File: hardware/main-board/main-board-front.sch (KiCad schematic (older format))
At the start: 25 parts

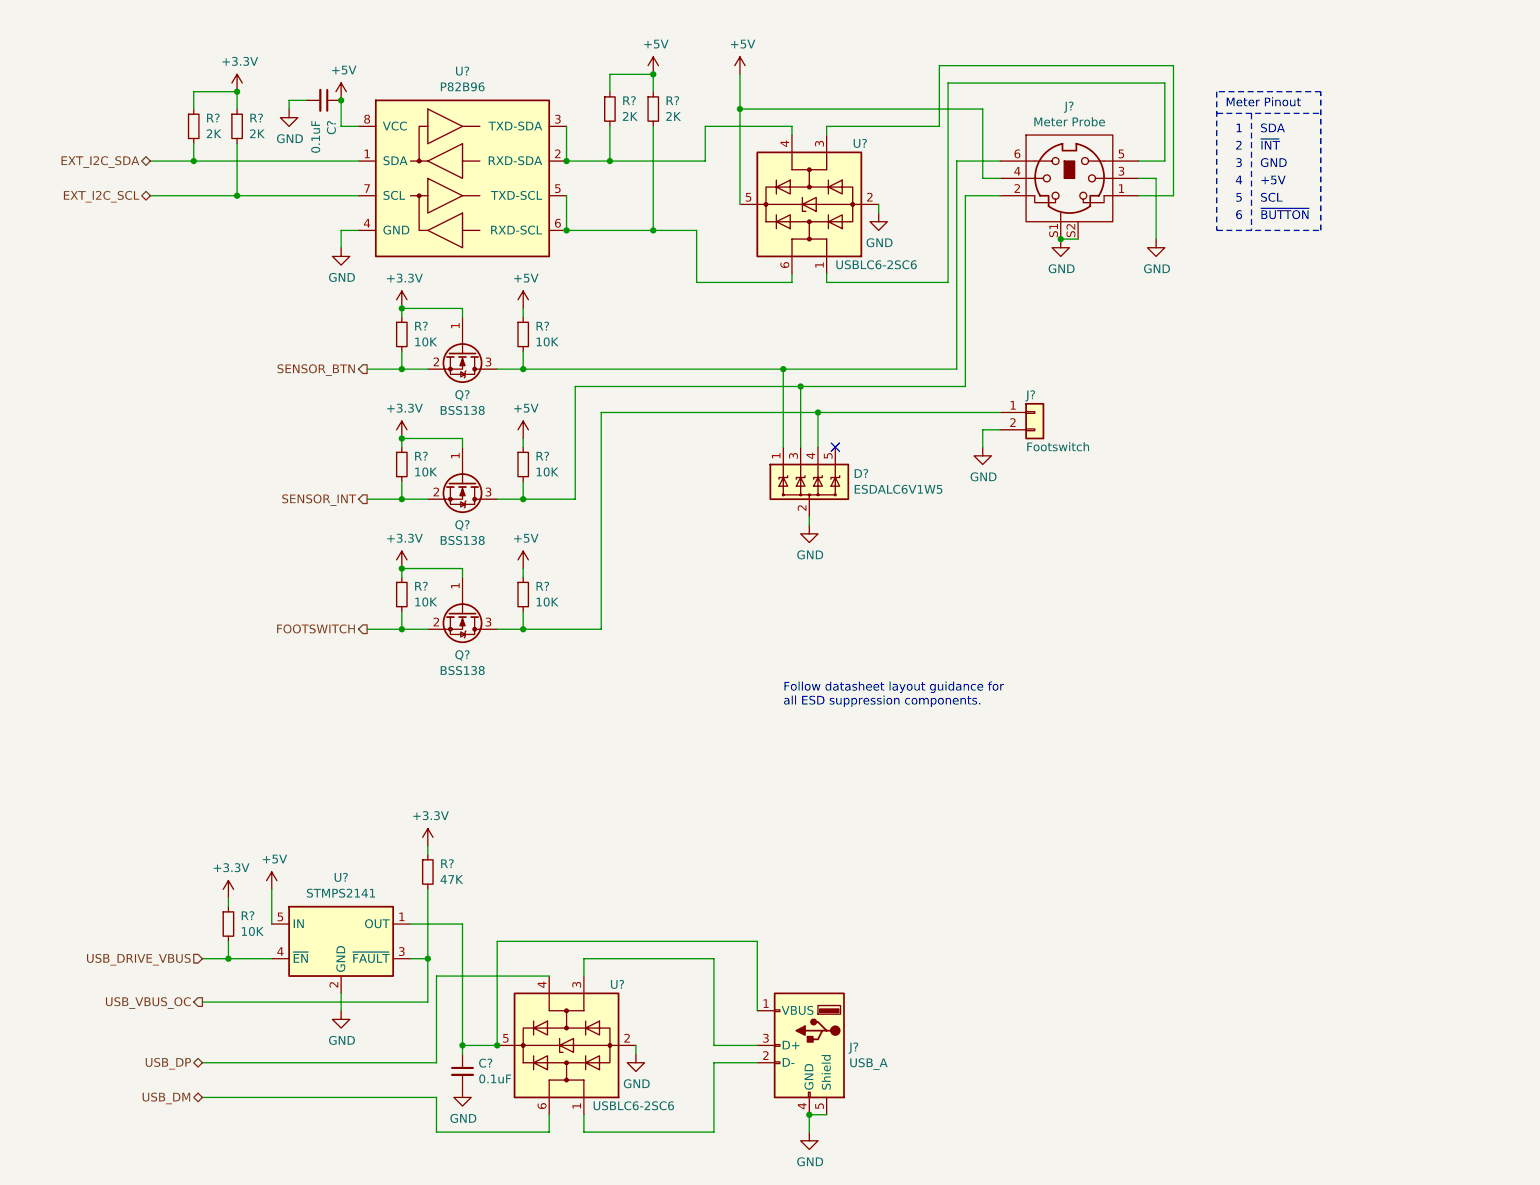
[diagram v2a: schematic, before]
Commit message: Annotated schematic got ERC to pass
Annotated a few components manually, then let KiCad to the rest
automatically.

Added no-connection flags to all intentionally-unused pins.
Added comments next to no-connection pins that are likely to become used
soon.
Fixed USB power switch schematic symbol's output pin type.
Fixed IEC output jack schematic symbol pin types.
Rearranged power flags as needed to get ERC to pass.

In cases where power needs to flow through another component (switch,
fuse, inductor, etc) a power flag is needed to make ERC happy.

The Vcap pin on the STM32 schematic symbol seems to be designated as a
power input, even though this pin is only supposed to connect to a
capacitor to ground. Added a power flag to make ERC happy here, to avoid
duplicating a library symbol.
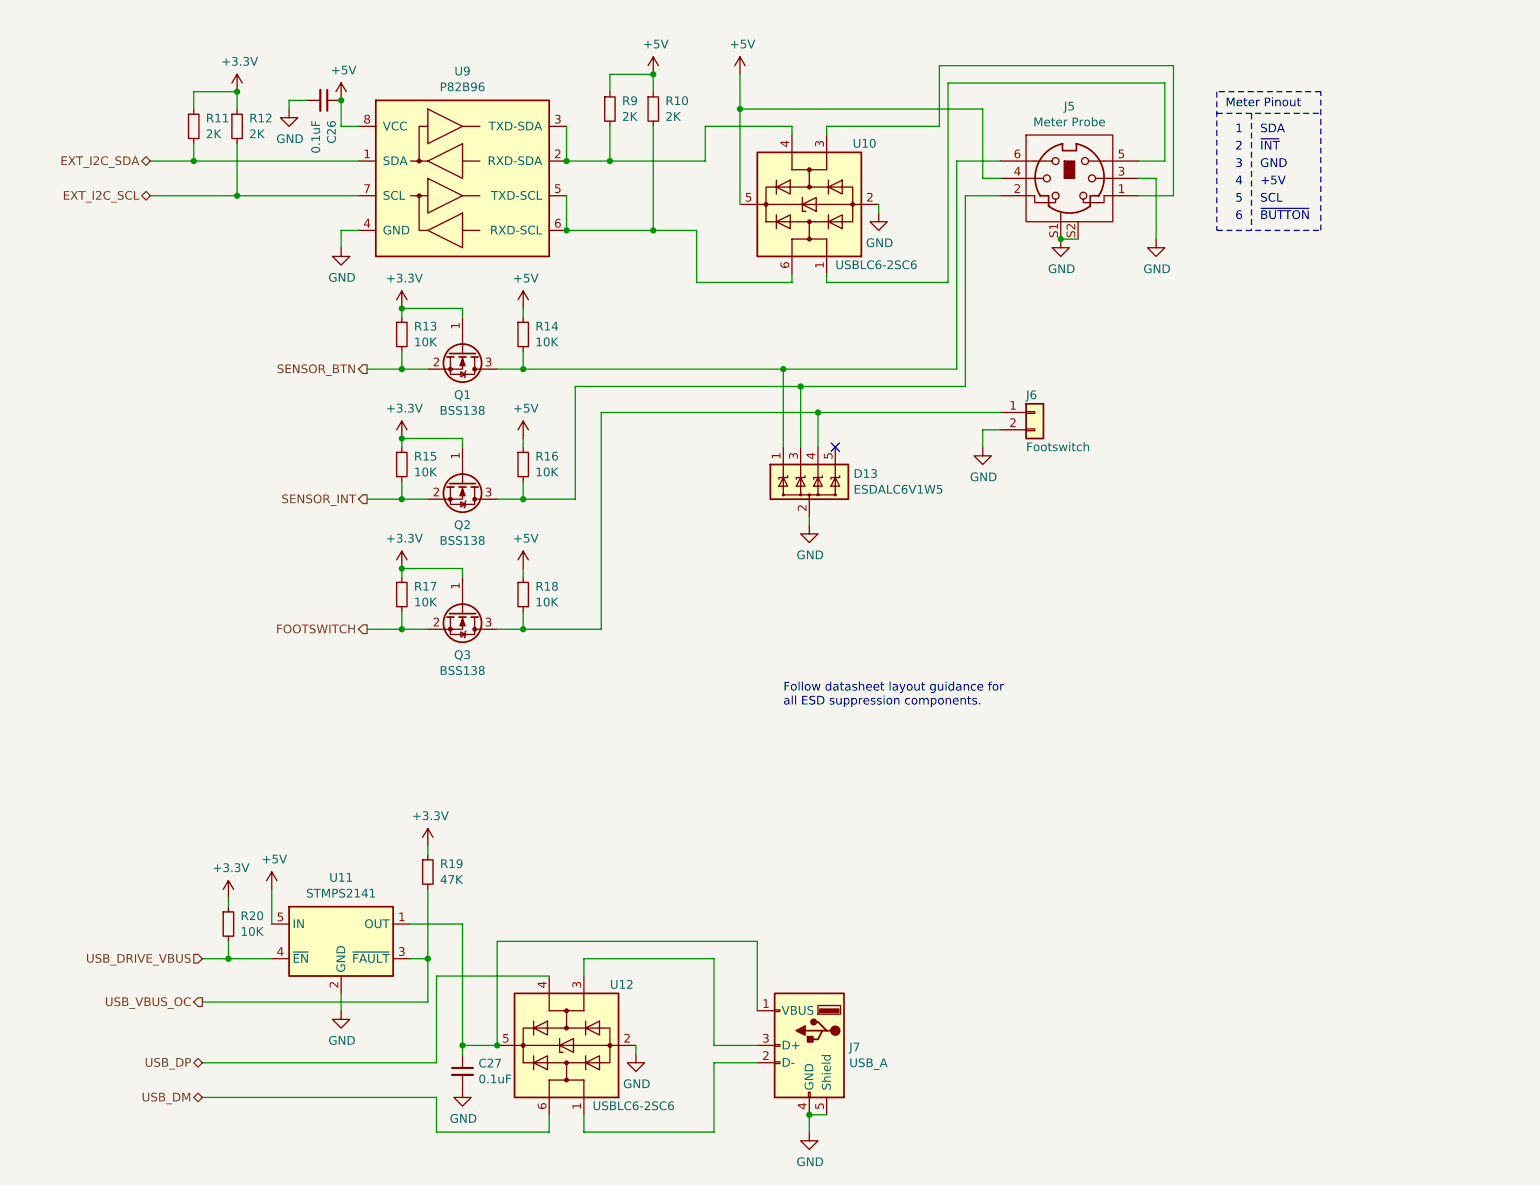
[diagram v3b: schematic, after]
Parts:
- gave numbers to parts that had none: 25
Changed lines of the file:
@@
 P 3150 1550
 AR Path="/5FA4F8E7" Ref="U?"  Part="1"
-AR Path="/5FA19AFF/5FA4F8E7" Ref="U?"  Part="1"
-F 0 "U?" H 3150 2167 50  0000 C CNN
+AR Path="/5FA19AFF/5FA4F8E7" Ref="U9"  Part="1"
+F 0 "U9" H 3150 2167 50  0000 C CNN
 F 1 "P82B96" H 3150 2076 50  0000 C CNN
 F 2 "" H 3150 1550 50  0001 C CNN
@@
 P 4250 1150
 AR Path="/5FA4F8F1" Ref="R?"  Part="1"
-AR Path="/5FA19AFF/5FA4F8F1" Ref="R?"  Part="1"
-F 0 "R?" H 4320 1196 50  0000 L CNN
+AR Path="/5FA19AFF/5FA4F8F1" Ref="R10"  Part="1"
+F 0 "R10" H 4320 1196 50  0000 L CNN
 F 1 "2K" H 4320 1105 50  0000 L CNN
 F 2 "" V 4180 1150 50  0001 C CNN
@@
 P 4000 1150
 AR Path="/5FA4F8F7" Ref="R?"  Part="1"
-AR Path="/5FA19AFF/5FA4F8F7" Ref="R?"  Part="1"
-F 0 "R?" H 4070 1196 50  0000 L CNN
+AR Path="/5FA19AFF/5FA4F8F7" Ref="R9"  Part="1"
+F 0 "R9" H 4070 1196 50  0000 L CNN
 F 1 "2K" H 4070 1105 50  0000 L CNN
 F 2 "" V 3930 1150 50  0001 C CNN
@@
 P 2350 1100
 AR Path="/5FA4F911" Ref="C?"  Part="1"
-AR Path="/5FA19AFF/5FA4F911" Ref="C?"  Part="1"
-F 0 "C?" H 2465 1146 50  0000 L CNN
+AR Path="/5FA19AFF/5FA4F911" Ref="C26"  Part="1"
+F 0 "C26" H 2465 1146 50  0000 L CNN
 F 1 "0.1uF" H 2465 1055 50  0000 L CNN
 F 2 "" H 2388 950 50  0001 C CNN
@@
 P 1850 1250
 AR Path="/5FA4F924" Ref="R?"  Part="1"
-AR Path="/5FA19AFF/5FA4F924" Ref="R?"  Part="1"
-F 0 "R?" H 1920 1296 50  0000 L CNN
+AR Path="/5FA19AFF/5FA4F924" Ref="R12"  Part="1"
+F 0 "R12" H 1920 1296 50  0000 L CNN
 F 1 "2K" H 1920 1205 50  0000 L CNN
 F 2 "" V 1780 1250 50  0001 C CNN
@@
 P 1600 1250
 AR Path="/5FA4F92A" Ref="R?"  Part="1"
-AR Path="/5FA19AFF/5FA4F92A" Ref="R?"  Part="1"
-F 0 "R?" H 1670 1296 50  0000 L CNN
+AR Path="/5FA19AFF/5FA4F92A" Ref="R11"  Part="1"
+F 0 "R11" H 1670 1296 50  0000 L CNN
 F 1 "2K" H 1670 1205 50  0000 L CNN
 F 2 "" V 1530 1250 50  0001 C CNN
@@
 P 6650 1550
 AR Path="/5FA4F940" Ref="J?"  Part="1"
-AR Path="/5FA19AFF/5FA4F940" Ref="J?"  Part="1"
-F 0 "J?" H 6650 1965 50  0000 C CNN
+AR Path="/5FA19AFF/5FA4F940" Ref="J5"  Part="1"
+F 0 "J5" H 6650 1965 50  0000 C CNN
 F 1 "Meter Probe" H 6650 1874 50  0000 C CNN
 F 2 "lib_fp:CUI_MD-60SM" H 6650 950 50  0001 C CNN
@@
 P 3150 2550
 AR Path="/5FA4F969" Ref="Q?"  Part="1"
-AR Path="/5FA19AFF/5FA4F969" Ref="Q?"  Part="1"
-F 0 "Q?" V 3399 2550 50  0000 C CNN
+AR Path="/5FA19AFF/5FA4F969" Ref="Q1"  Part="1"
+F 0 "Q1" V 3399 2550 50  0000 C CNN
 F 1 "BSS138" V 3490 2550 50  0000 C CNN
 F 2 "Package_TO_SOT_SMD:SOT-23" H 3350 2475 50  0001 L CIN
@@
 P 3150 3300
 AR Path="/5FA4F96F" Ref="Q?"  Part="1"
-AR Path="/5FA19AFF/5FA4F96F" Ref="Q?"  Part="1"
-F 0 "Q?" V 3399 3300 50  0000 C CNN
+AR Path="/5FA19AFF/5FA4F96F" Ref="Q2"  Part="1"
+F 0 "Q2" V 3399 3300 50  0000 C CNN
 F 1 "BSS138" V 3490 3300 50  0000 C CNN
 F 2 "Package_TO_SOT_SMD:SOT-23" H 3350 3225 50  0001 L CIN
@@
 P 2800 2450
 AR Path="/5FA4F975" Ref="R?"  Part="1"
-AR Path="/5FA19AFF/5FA4F975" Ref="R?"  Part="1"
-F 0 "R?" H 2870 2496 50  0000 L CNN
+AR Path="/5FA19AFF/5FA4F975" Ref="R13"  Part="1"
+F 0 "R13" H 2870 2496 50  0000 L CNN
 F 1 "10K" H 2870 2405 50  0000 L CNN
 F 2 "" V 2730 2450 50  0001 C CNN
@@
 P 3500 2450
 AR Path="/5FA4F97B" Ref="R?"  Part="1"
-AR Path="/5FA19AFF/5FA4F97B" Ref="R?"  Part="1"
-F 0 "R?" H 3570 2496 50  0000 L CNN
+AR Path="/5FA19AFF/5FA4F97B" Ref="R14"  Part="1"
+F 0 "R14" H 3570 2496 50  0000 L CNN
 F 1 "10K" H 3570 2405 50  0000 L CNN
 F 2 "" V 3430 2450 50  0001 C CNN
@@
 P 2800 3200
 AR Path="/5FA4F981" Ref="R?"  Part="1"
-AR Path="/5FA19AFF/5FA4F981" Ref="R?"  Part="1"
-F 0 "R?" H 2870 3246 50  0000 L CNN
+AR Path="/5FA19AFF/5FA4F981" Ref="R15"  Part="1"
+F 0 "R15" H 2870 3246 50  0000 L CNN
 F 1 "10K" H 2870 3155 50  0000 L CNN
 F 2 "" V 2730 3200 50  0001 C CNN
@@
 P 3500 3200
 AR Path="/5FA4F987" Ref="R?"  Part="1"
-AR Path="/5FA19AFF/5FA4F987" Ref="R?"  Part="1"
-F 0 "R?" H 3570 3246 50  0000 L CNN
+AR Path="/5FA19AFF/5FA4F987" Ref="R16"  Part="1"
+F 0 "R16" H 3570 3246 50  0000 L CNN
 F 1 "10K" H 3570 3155 50  0000 L CNN
 F 2 "" V 3430 3200 50  0001 C CNN
@@
 P 3750 6550
 AR Path="/5FA5B3D0" Ref="U?"  Part="1"
-AR Path="/5FA19AFF/5FA5B3D0" Ref="U?"  Part="1"
-F 0 "U?" V 4100 6300 50  0000 R CNN
+AR Path="/5FA19AFF/5FA5B3D0" Ref="U12"  Part="1"
+F 0 "U12" V 4100 6300 50  0000 R CNN
 F 1 "USBLC6-2SC6" V 3400 6400 50  0000 R CNN
 F 2 "Package_TO_SOT_SMD:SOT-23-6" H 3750 6050 50  0001 C CNN
@@
 P 2450 5950
 AR Path="/5FA5B3D6" Ref="U?"  Part="1"
-AR Path="/5FA19AFF/5FA5B3D6" Ref="U?"  Part="1"
-F 0 "U?" H 2450 6317 50  0000 C CNN
+AR Path="/5FA19AFF/5FA5B3D6" Ref="U11"  Part="1"
+F 0 "U11" H 2450 6317 50  0000 C CNN
 F 1 "STMPS2141" H 2450 6226 50  0000 C CNN
 F 2 "Package_TO_SOT_SMD:SOT-23-5" H 2450 6300 50  0001 C CNN
@@
 P 5150 6550
 AR Path="/5FA5B3DC" Ref="J?"  Part="1"
-AR Path="/5FA19AFF/5FA5B3DC" Ref="J?"  Part="1"
-F 0 "J?" H 4920 6539 50  0000 R CNN
+AR Path="/5FA19AFF/5FA5B3DC" Ref="J7"  Part="1"
+F 0 "J7" H 4920 6539 50  0000 R CNN
 F 1 "USB_A" H 4920 6448 50  0000 R CNN
 F 2 "" H 5300 6500 50  0001 C CNN
@@
 P 2950 5550
 AR Path="/5FA5B407" Ref="R?"  Part="1"
-AR Path="/5FA19AFF/5FA5B407" Ref="R?"  Part="1"
-F 0 "R?" H 3020 5596 50  0000 L CNN
+AR Path="/5FA19AFF/5FA5B407" Ref="R19"  Part="1"
+F 0 "R19" H 3020 5596 50  0000 L CNN
 F 1 "47K" H 3020 5505 50  0000 L CNN
 F 2 "" V 2880 5550 50  0001 C CNN
@@
 P 1800 5850
 AR Path="/5FA5B416" Ref="R?"  Part="1"
-AR Path="/5FA19AFF/5FA5B416" Ref="R?"  Part="1"
-F 0 "R?" H 1870 5896 50  0000 L CNN
+AR Path="/5FA19AFF/5FA5B416" Ref="R20"  Part="1"
+F 0 "R20" H 1870 5896 50  0000 L CNN
 F 1 "10K" H 1870 5805 50  0000 L CNN
 F 2 "" V 1730 5850 50  0001 C CNN
@@
 	3000 6850 1650 6850
 $Comp
-L Device:C_Small C?
+L Device:C_Small C27
 U 1 1 5F988495
 P 3150 6700
-F 0 "C?" H 3242 6746 50  0000 L CNN
+F 0 "C27" H 3242 6746 50  0000 L CNN
 F 1 "0.1uF" H 3242 6655 50  0000 L CNN
 F 2 "" H 3150 6700 50  0001 C CNN
@@
 	3000 7050 3000 6850
 $Comp
-L Connector_Generic:Conn_01x02 J?
+L Connector_Generic:Conn_01x02 J6
 U 1 1 5F9A4F1A
 P 6450 2900
-F 0 "J?" H 6400 3000 50  0000 L CNN
+F 0 "J6" H 6400 3000 50  0000 L CNN
 F 1 "Footswitch" H 6400 2700 50  0000 L CNN
 F 2 "Connector_PinHeader_2.54mm:PinHeader_1x02_P2.54mm_Vertical" H 6450 2900 50  0001 C CNN
@@
 P 6150 3100
 AR Path="/5F9B6C01" Ref="#PWR?"  Part="1"
-AR Path="/5FA19AFF/5F9B6C01" Ref="#PWR?"  Part="1"
-F 0 "#PWR?" H 6150 2850 50  0001 C CNN
+AR Path="/5FA19AFF/5F9B6C01" Ref="#PWR071"  Part="1"
+F 0 "#PWR071" H 6150 2850 50  0001 C CNN
 F 1 "GND" H 6155 2927 50  0000 C CNN
 F 2 "" H 6150 3100 50  0001 C CNN
@@
 P 3150 4050
 AR Path="/5F9C71D7" Ref="Q?"  Part="1"
-AR Path="/5FA19AFF/5F9C71D7" Ref="Q?"  Part="1"
-F 0 "Q?" V 3399 4050 50  0000 C CNN
+AR Path="/5FA19AFF/5F9C71D7" Ref="Q3"  Part="1"
+F 0 "Q3" V 3399 4050 50  0000 C CNN
 F 1 "BSS138" V 3490 4050 50  0000 C CNN
 F 2 "Package_TO_SOT_SMD:SOT-23" H 3350 3975 50  0001 L CIN
@@
 P 2800 3950
 AR Path="/5F9C76EB" Ref="R?"  Part="1"
-AR Path="/5FA19AFF/5F9C76EB" Ref="R?"  Part="1"
-F 0 "R?" H 2870 3996 50  0000 L CNN
+AR Path="/5FA19AFF/5F9C76EB" Ref="R17"  Part="1"
+F 0 "R17" H 2870 3996 50  0000 L CNN
 F 1 "10K" H 2870 3905 50  0000 L CNN
 F 2 "" V 2730 3950 50  0001 C CNN
@@
 P 3500 3950
 AR Path="/5F9C76F5" Ref="R?"  Part="1"
-AR Path="/5FA19AFF/5F9C76F5" Ref="R?"  Part="1"
-F 0 "R?" H 3570 3996 50  0000 L CNN
+AR Path="/5FA19AFF/5F9C76F5" Ref="R18"  Part="1"
+F 0 "R18" H 3570 3996 50  0000 L CNN
 F 1 "10K" H 3570 3905 50  0000 L CNN
 F 2 "" V 3430 3950 50  0001 C CNN
@@
 P 2800 3800
 AR Path="/5F9C76FF" Ref="#PWR?"  Part="1"
-AR Path="/5FA19AFF/5F9C76FF" Ref="#PWR?"  Part="1"
-F 0 "#PWR?" H 2800 3650 50  0001 C CNN
+AR Path="/5FA19AFF/5F9C76FF" Ref="#PWR073"  Part="1"
+F 0 "#PWR073" H 2800 3650 50  0001 C CNN
 F 1 "+3.3V" H 2815 3973 50  0000 C CNN
 F 2 "" H 2800 3800 50  0001 C CNN
@@
 P 3500 3800
 AR Path="/5F9C7709" Ref="#PWR?"  Part="1"
-AR Path="/5FA19AFF/5F9C7709" Ref="#PWR?"  Part="1"
-F 0 "#PWR?" H 3500 3650 50  0001 C CNN
+AR Path="/5FA19AFF/5F9C7709" Ref="#PWR074"  Part="1"
+F 0 "#PWR074" H 3500 3650 50  0001 C CNN
 F 1 "+5V" H 3515 3973 50  0000 C CNN
 F 2 "" H 3500 3800 50  0001 C CNN
@@
 Connection ~ 2800 4150
 $Comp
-L Project:ESDALC6V1W5 D?
+L Project:ESDALC6V1W5 D13
 U 1 1 5F9DF2EA
 P 5150 3300
-F 0 "D?" V 5104 3555 50  0000 L CNN
+F 0 "D13" V 5104 3555 50  0000 L CNN
 F 1 "ESDALC6V1W5" V 5195 3555 50  0000 L CNN
 F 2 "lib_fp:SOT323-5L" H 5150 2925 50  0001 C CNN
@@
 P 5150 1700
 AR Path="/5F9E0AB3" Ref="U?"  Part="1"
-AR Path="/5FA19AFF/5F9E0AB3" Ref="U?"  Part="1"
-F 0 "U?" V 5500 1450 50  0000 R CNN
+AR Path="/5FA19AFF/5F9E0AB3" Ref="U10"  Part="1"
+F 0 "U10" V 5500 1450 50  0000 R CNN
 F 1 "USBLC6-2SC6" V 4800 1550 50  0000 R CNN
 F 2 "Package_TO_SOT_SMD:SOT-23-6" H 5150 1200 50  0001 C CNN
@@
 P 5550 1750
 AR Path="/5FA27F45" Ref="#PWR?"  Part="1"
-AR Path="/5FA19AFF/5FA27F45" Ref="#PWR?"  Part="1"
-F 0 "#PWR?" H 5550 1500 50  0001 C CNN
+AR Path="/5FA19AFF/5FA27F45" Ref="#PWR070"  Part="1"
+F 0 "#PWR070" H 5550 1500 50  0001 C CNN
 F 1 "GND" H 5555 1577 50  0000 C CNN
 F 2 "" H 5550 1750 50  0001 C CNN
@@
 P 5150 3550
 AR Path="/5FA61E9F" Ref="#PWR?"  Part="1"
-AR Path="/5FA19AFF/5FA61E9F" Ref="#PWR?"  Part="1"
-F 0 "#PWR?" H 5150 3300 50  0001 C CNN
+AR Path="/5FA19AFF/5FA61E9F" Ref="#PWR072"  Part="1"
+F 0 "#PWR072" H 5150 3300 50  0001 C CNN
 F 1 "GND" H 5155 3377 50  0000 C CNN
 F 2 "" H 5150 3550 50  0001 C CNN

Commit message: Fill in BOM data for all known components
Added BOM assignments for main board components
Fixed GNDDetect connection on STDC14 connector

Added more notes to the main board schematic of things that are still
TBD or need fixing.
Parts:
- C26, C27: footprint (none) -> Capacitor_SMD:C_0603_1608Metric; Description (none) -> CAP CER 0.1UF 25V X7R 0603; Manufacturer (none) -> Samsung Electro-Mechanics; Manufacturer PN (none) -> CL10B104KA8NNNC; Supplier (none) -> Digi-Key; Supplier PN (none) -> 1276-1006-1-ND
- D13: Description (none) -> TVS DIODE 3V SOT323-5; Manufacturer (none) -> STMicroelectronics; Manufacturer PN (none) -> ESDALC6V1W5; Supplier (none) -> Digi-Key; Supplier PN (none) -> 497-7231-1-ND
- J6: footprint Connector_PinHeader_2.54mm:PinHeader_1x02_P2.54mm_Vertical -> Connector_JST:JST_PH_B2B-PH-K_1x02_P2.00mm_Vertical; Description (none) -> CONN HEADER VERT 2POS 2MM; Manufacturer (none) -> JST Sales America Inc.; Manufacturer PN (none) -> B2B-PH-K-S(LF)(SN); Supplier (none) -> Digi-Key; Supplier PN (none) -> 455-1704-ND
- J7: footprint (none) -> Connector_USB:USB_A_Molex_67643_Horizontal; Description (none) -> CONN RCPT TYPEA 4POS R/A; Manufacturer (none) -> Molex; Manufacturer PN (none) -> 0676432910; Supplier (none) -> Digi-Key; Supplier PN (none) -> WM11258-ND
- Q1, Q2, Q3: Description (none) -> MOSFET N-CH 50V 220MA SOT-23; Manufacturer (none) -> ON Semiconductor; Manufacturer PN (none) -> BSS138; Supplier (none) -> Digi-Key; Supplier PN (none) -> BSS138CT-ND
- R10, R11, R12, R9: footprint (none) -> Resistor_SMD:R_0603_1608Metric; Description (none) -> RES SMD 2K OHM 5% 1/10W 0603; Manufacturer (none) -> Vishay Dale; Manufacturer PN (none) -> CRCW06032K00JNEA; Supplier (none) -> Digi-Key; Supplier PN (none) -> 541-2.0KGCT-ND
- R13, R14, R15, R16, R17, R18, R20: footprint (none) -> Resistor_SMD:R_0603_1608Metric; Description (none) -> RES SMD 10K OHM 5% 1/10W 0603; Manufacturer (none) -> Vishay Dale; Manufacturer PN (none) -> CRCW060310K0JNEA; Supplier (none) -> Digi-Key; Supplier PN (none) -> 541-10KGCT-ND
- R19: footprint (none) -> Resistor_SMD:R_0603_1608Metric; Description (none) -> RES 47K OHM 5% 1/10W 0603; Manufacturer (none) -> Vishay Dale; Manufacturer PN (none) -> CRCW060347K0JNEAC; Supplier (none) -> Digi-Key; Supplier PN (none) -> 541-4061-1-ND
- U10, U12: Description (none) -> TVS DIODE 5.25V 17V SOT23-6; Manufacturer (none) -> STMicroelectronics; Manufacturer PN (none) -> USBLC6-2SC6; Supplier (none) -> Digi-Key; Supplier PN (none) -> 497-5235-1-ND
- U11: Description (none) -> IC PWR SWITCH N-CHAN 1:1 SOT23-5; Manufacturer (none) -> STMicroelectronics; Manufacturer PN (none) -> STMPS2141STR; Supplier (none) -> Digi-Key; Supplier PN (none) -> 497-6933-1-ND
- U9: footprint (none) -> Package_SO:SOIC-8_3.9x4.9mm_P1.27mm; Description (none) -> IC REDRIVER I2C 1CH 400KHZ 8SOIC; Manufacturer (none) -> Texas Instruments; Manufacturer PN (none) -> P82B96DR; Supplier (none) -> Digi-Key; Supplier PN (none) -> 296-20942-1-ND
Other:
- note added: "TVS array likely has wrong\nclamping voltage here"
